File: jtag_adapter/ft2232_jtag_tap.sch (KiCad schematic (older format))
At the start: 50 parts, among them J1 USB_C_Receptacle_USB2.0, J2 Conn_ARM_JTAG_SWD_20, U1 93AA56BT-I/OT, U2 FT232HL, Y1 Crystal_GND24

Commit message: v0.2に改修
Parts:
- removed D1, D2: PGB1010603, Diode_SMD:D_0603_1608Metric, symbol Diode:ESD9B5.0ST5G
- removed R11, R12, R13, R14, R15, R16, R17, R7, R8: 0, Resistor_SMD:R_0603_1608Metric, symbol Device:R
- added D1: PWR_LED, LED_SMD:LED_0603_1608Metric, symbol Device:LED
- added R9: 1k, Resistor_SMD:R_0603_1608Metric, symbol Device:R
- J2: footprint Connector_PinHeader_2.54mm:PinHeader_2x10_P2.54mm_Horizontal -> Connector_IDC:IDC-Header_2x10_P2.54mm_Horizontal
- R8: renamed from R10; value 10k -> 12k/1%
- renumbered R9 to R7
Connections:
- wire segments 198 -> 185
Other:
- note added: "Bypass capacitors for FT232HL"
- note added: "for VCCIO(3.3v)"
- note removed: "Bypass capacitors for FT2232"
- note removed: "dumping resistors"

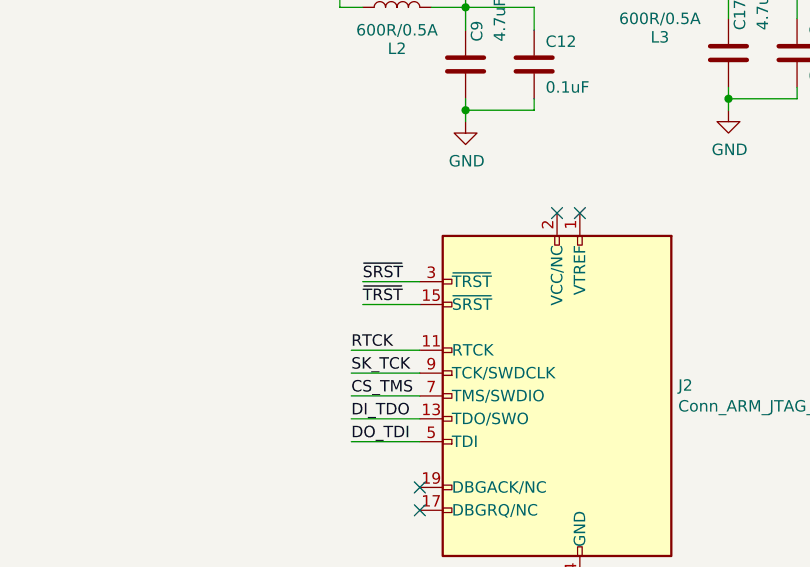
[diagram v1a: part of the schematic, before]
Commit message: fix SRST/TRST and remove unnecessary files
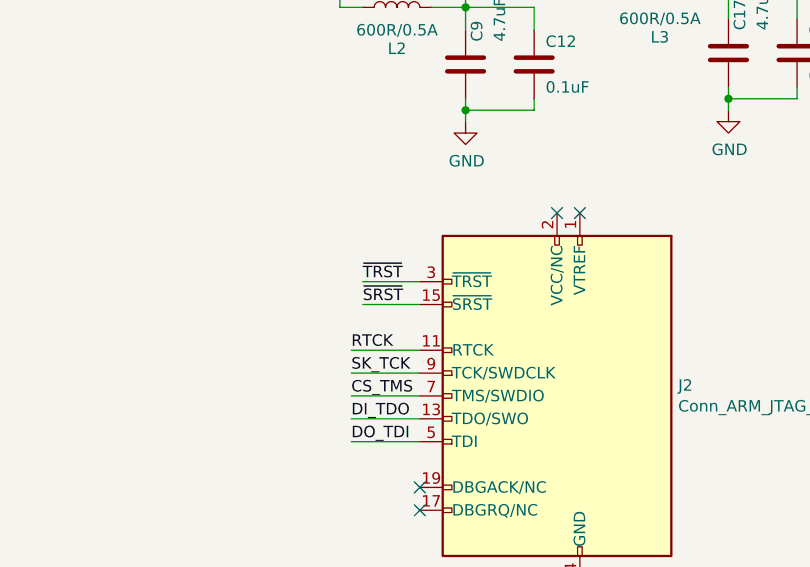
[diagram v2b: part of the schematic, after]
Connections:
- net ~SRST: now also J2.15 (~SRST~); no longer J2.3 (~TRST~)
- net ~TRST: now also J2.3 (~TRST~); no longer J2.15 (~SRST~)
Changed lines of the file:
@@
 Text Label 7650 2650 2    50   ~ 0
 ~TRST
+Text Label 8850 4700 0    50   ~ 0
+~SRST
 Text Label 8850 4600 0    50   ~ 0
-~SRST
-Text Label 8850 4700 0    50   ~ 0
 ~TRST
 Wire Wire Line

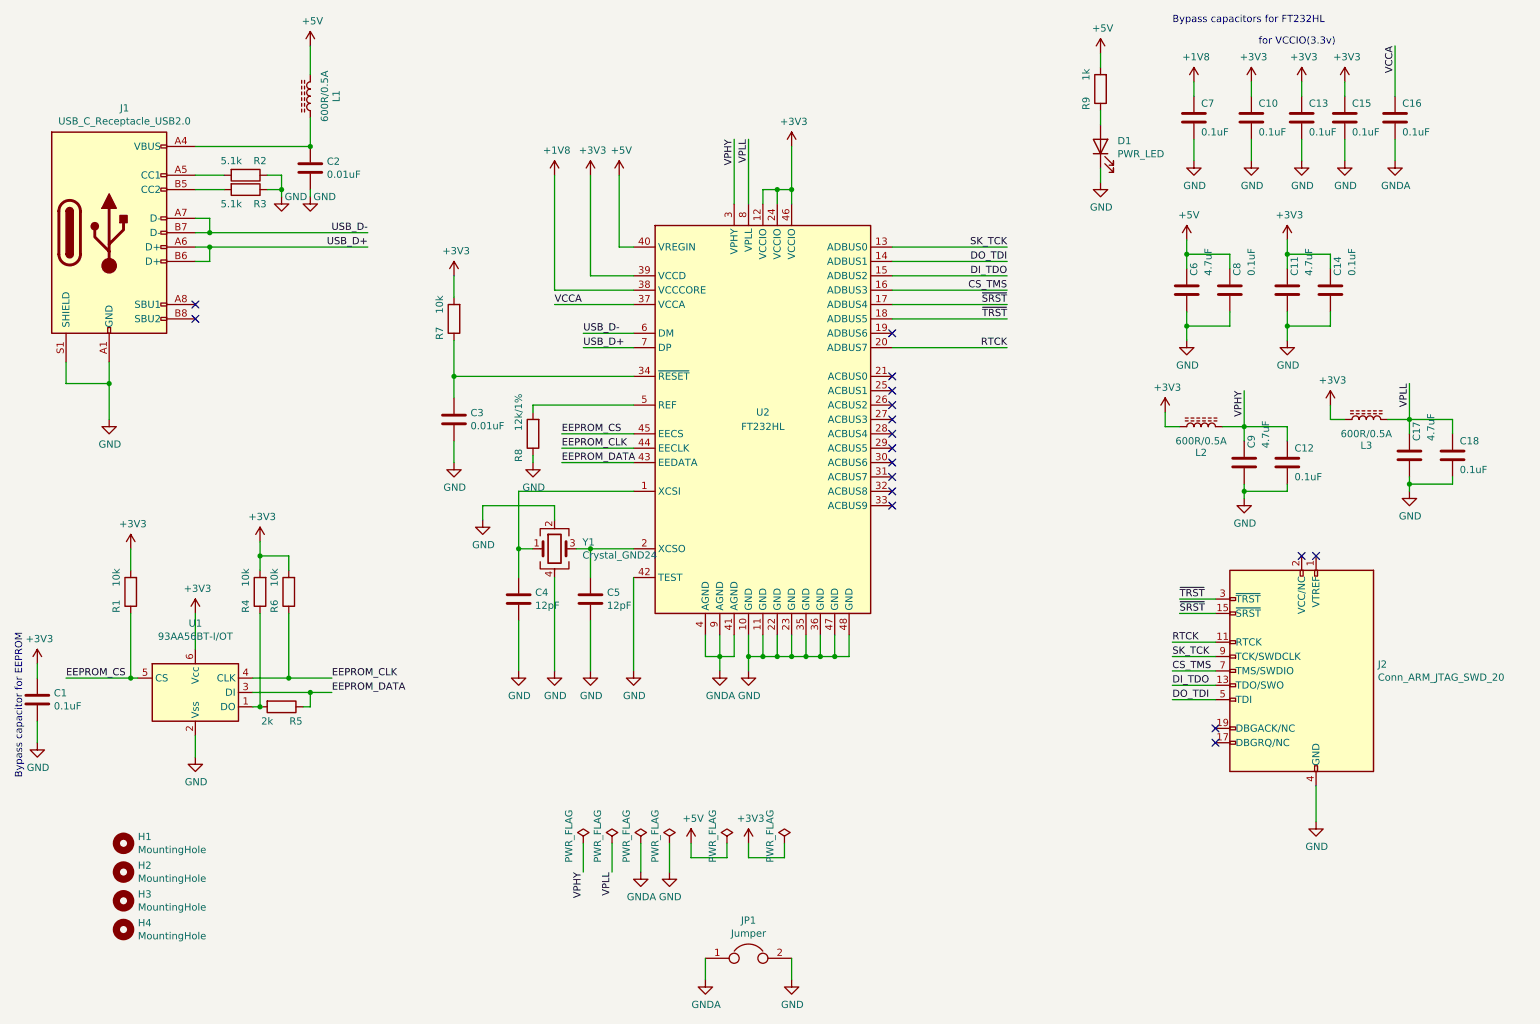
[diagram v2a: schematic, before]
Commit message: wip: 回路図の改善とレベル変換ICの追加
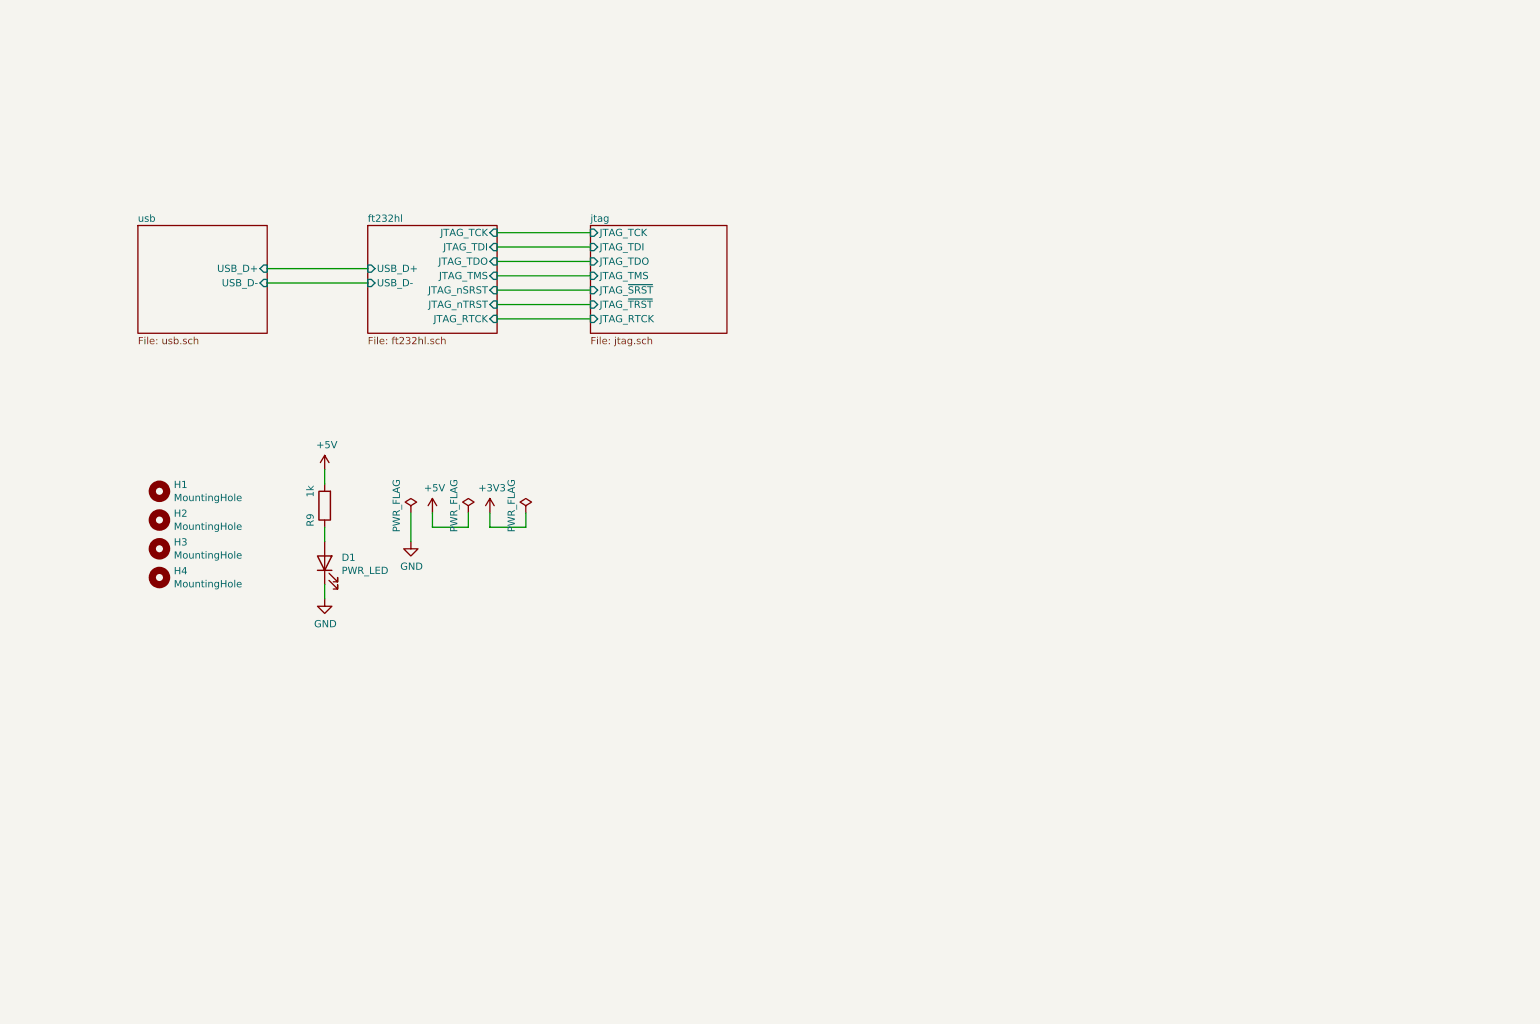
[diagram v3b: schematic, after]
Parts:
- removed C1, C10, C12, C13, C14, C15, C16, C18, C7, C8: 0.1uF, Capacitor_SMD:C_0603_1608Metric, symbol Device:C
- removed C11, C17, C6, C9: 4.7uF, Capacitor_SMD:C_0603_1608Metric, symbol Device:C
- removed C2, C3: 0.01uF, Capacitor_SMD:C_0603_1608Metric, symbol Device:C
- removed C4, C5: 12pF, Capacitor_SMD:C_0603_1608Metric, symbol Device:C
- removed J1: USB_C_Receptacle_USB2.0, Connector_USB:USB_C_Receptacle_GCT_USB4085, symbol Connector:USB_C_Receptacle_USB2.0
- removed J2: Conn_ARM_JTAG_SWD_20, Connector_IDC:IDC-Header_2x10_P2.54mm_Horizontal, symbol Connector:Conn_ARM_JTAG_SWD_20
- removed JP1: Jumper, Jumper:SolderJumper-2_P1.3mm_Bridged_Pad1.0x1.5mm, symbol Device:Jumper
- removed L1, L2, L3: 600R/0.5A, Inductor_SMD:L_0603_1608Metric, symbol Device:L_Core_Ferrite
- removed R1, R4, R6, R7: 10k, Resistor_SMD:R_0603_1608Metric, symbol Device:R
- removed R2, R3: 5.1k, Resistor_SMD:R_0603_1608Metric, symbol Device:R
- removed R5: 2k, Resistor_SMD:R_0603_1608Metric, symbol Device:R
- removed R8: 12k/1%, Resistor_SMD:R_0603_1608Metric, symbol Device:R
- removed U1: 93AA56BT-I/OT, Package_TO_SOT_SMD:SOT-23-6, symbol Memory_EEPROM:93AAxxBT-xOT
- removed U2: FT232HL, Package_QFP:LQFP-48-1EP_7x7mm_P0.5mm_EP3.6x3.6mm, symbol Interface_USB:FT232H
- removed Y1: Crystal_GND24, Crystal:Crystal_SMD_SeikoEpson_FA238-4Pin_3.2x2.5mm, symbol Device:Crystal_GND24
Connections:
- no-connect marks 17 -> 0
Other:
- note removed: "Bypass capacitor for EEPROM"
- note removed: "Bypass capacitors for FT232HL"
- note removed: "for VCCIO(3.3v)"
- moved on the sheet: D1, H1, H2, H3, H4, R9

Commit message: wip
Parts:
- added L1: 600R/0.5A, Inductor_SMD:L_0603_1608Metric, symbol Device:L_Core_Ferrite
- added TP1, TP2, TP3: TestPoint, TestPoint:TestPoint_Pad_D1.0mm, symbol Connector:TestPoint
- renumbered R9 to R1
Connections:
- net +3V3: now also TP3.1
- net +5V: now also TP2.1
- net GND: now also L1.1, TP1.1
- new net GNDA: L1.2
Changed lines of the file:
@@
 encoding utf-8
 Sheet 1 4
-Title ""
-Date ""
-Rev ""
-Comp ""
+Title "FT232 JTAG adapter"
+Date "2021-09-01"
+Rev "v1.0"
+Comp "Toshifumi NISHINAGA(@tnishinaga)"
 Comment1 ""
 Comment2 ""
@@
 $EndDescr
 $Comp
-L power:+5V #PWR023
+L power:+5V #PWR07
 U 1 1 60945E93
-P 3650 4000
-F 0 "#PWR023" H 3650 3850 50  0001 C CNN
-F 1 "+5V" H 3665 4173 50  0000 C CNN
-F 2 "" H 3650 4000 50  0001 C CNN
-F 3 "" H 3650 4000 50  0001 C CNN
-	1    3650 4000
-	1    0    0    -1
+P 4250 4000
+F 0 "#PWR07" H 4250 3850 50  0001 C CNN
+F 1 "+5V" H 4265 4173 50  0000 C CNN
+F 2 "" H 4250 4000 50  0001 C CNN
+F 3 "" H 4250 4000 50  0001 C CNN
+	1    4250 4000
+	1    0    0    -1
+$EndComp
+$Comp
+L power:PWR_FLAG #FLG03
+U 1 1 609471DE
+P 4250 4200
+F 0 "#FLG03" H 4250 4275 50  0001 C CNN
+F 1 "PWR_FLAG" V 4150 4300 50  0000 C CNN
+F 2 "" H 4250 4200 50  0001 C CNN
+F 3 "~" H 4250 4200 50  0001 C CNN
+	1    4250 4200
+	-1   0    0    1
 $EndComp
 $Comp
 L power:PWR_FLAG #FLG04
-U 1 1 609471DE
-P 3900 4000
-F 0 "#FLG04" H 3900 4075 50  0001 C CNN
-F 1 "PWR_FLAG" V 3800 4050 50  0000 C CNN
-F 2 "" H 3900 4000 50  0001 C CNN
-F 3 "~" H 3900 4000 50  0001 C CNN
-	1    3900 4000
-	1    0    0    -1
-$EndComp
-Wire Wire Line
-	3650 4000 3650 4100
-Wire Wire Line
-	3650 4100 3900 4100
-Wire Wire Line
-	3900 4100 3900 4000
-$Comp
-L power:PWR_FLAG #FLG05
 U 1 1 60951BF8
-P 4300 4000
-F 0 "#FLG05" H 4300 4075 50  0001 C CNN
-F 1 "PWR_FLAG" V 4200 4050 50  0000 C CNN
-F 2 "" H 4300 4000 50  0001 C CNN
-F 3 "~" H 4300 4000 50  0001 C CNN
-	1    4300 4000
-	1    0    0    -1
-$EndComp
-$Comp
-L power:+3V3 #PWR027
+P 4700 4200
+F 0 "#FLG04" H 4700 4275 50  0001 C CNN
+F 1 "PWR_FLAG" V 4600 4300 50  0000 C CNN
+F 2 "" H 4700 4200 50  0001 C CNN
+F 3 "~" H 4700 4200 50  0001 C CNN
+	1    4700 4200
+	-1   0    0    1
+$EndComp
+$Comp
+L power:+3V3 #PWR08
 U 1 1 60951E6D
-P 4050 4000
-F 0 "#PWR027" H 4050 3850 50  0001 C CNN
-F 1 "+3V3" H 4065 4173 50  0000 C CNN
-F 2 "" H 4050 4000 50  0001 C CNN
-F 3 "" H 4050 4000 50  0001 C CNN
-	1    4050 4000
-	1    0    0    -1
-$EndComp
-Wire Wire Line
-	4050 4000 4050 4100
-Wire Wire Line
-	4050 4100 4300 4100
-Wire Wire Line
-	4300 4100 4300 4000
+P 4700 4000
+F 0 "#PWR08" H 4700 3850 50  0001 C CNN
+F 1 "+3V3" H 4715 4173 50  0000 C CNN
+F 2 "" H 4700 4000 50  0001 C CNN
+F 3 "" H 4700 4000 50  0001 C CNN
+	1    4700 4000
+	1    0    0    -1
+$EndComp
 $Comp
 L Mechanical:MountingHole H1
@@
 $EndSheet
 $Sheet
-S 3200 2000 900  750
+S 3200 2000 900  1000
 U 61247445
 F0 "ft232hl" 50
@@
 F9 "JTAG_nTRST" I R 4100 2550 50
 F10 "JTAG_RTCK" I R 4100 2650 50
+F11 "SWDIO_OE" I R 4100 2750 50
+F12 "SWD_EN" I R 4100 2850 50
+F13 "JTAG_EN" I R 4100 2950 50
 $EndSheet
 Wire Wire Line
@@
 	3200 2400 2500 2400
 $Sheet
-S 4750 2000 950  750
+S 4750 2000 950  1000
 U 613347ED
 F0 "jtag" 50
@@
 F7 "JTAG_TDO" I L 4750 2250 50
 F8 "JTAG_TDI" I L 4750 2150 50
+F9 "SWDIO_OE" I L 4750 2750 50
+F10 "SWD_EN" I L 4750 2850 50
+F11 "JTAG_EN" I L 4750 2950 50
 $EndSheet
 Wire Wire Line
@@
 	4100 2650 4750 2650
 $Comp
-L power:+5V #PWR030
+L power:+5V #PWR01
 U 1 1 60F3D407
 P 2900 3700
-F 0 "#PWR030" H 2900 3550 50  0001 C CNN
+F 0 "#PWR01" H 2900 3550 50  0001 C CNN
 F 1 "+5V" H 2915 3873 50  0000 C CNN
 F 2 "" H 2900 3700 50  0001 C CNN
@@
 	2900 3700 2900 3800
 $Comp
-L power:GND #PWR031
+L power:GND #PWR02
 U 1 1 60F214BE
 P 2900 4600
-F 0 "#PWR031" H 2900 4350 50  0001 C CNN
+F 0 "#PWR02" H 2900 4350 50  0001 C CNN
 F 1 "GND" H 2905 4427 50  0000 C CNN
 F 2 "" H 2900 4600 50  0001 C CNN
@@
 $EndComp
 $Comp
-L Device:R R9
+L Device:R R1
 U 1 1 60F1735E
 P 2900 3950
-F 0 "R9" V 3000 4050 50  0000 C CNN
+F 0 "R1" V 3000 4050 50  0000 C CNN
 F 1 "1k" V 3000 3850 50  0000 C CNN
 F 2 "Resistor_SMD:R_0603_1608Metric" V 2830 3950 50  0001 C CNN
@@
 $EndComp
 $Comp
-L power:GND #PWR022
+L power:GND #PWR03
 U 1 1 6093156D
 P 3500 4200
-F 0 "#PWR022" H 3500 3950 50  0001 C CNN
+F 0 "#PWR03" H 3500 3950 50  0001 C CNN
 F 1 "GND" H 3505 4027 50  0000 C CNN
 F 2 "" H 3500 4200 50  0001 C CNN
@@
 $EndComp
 Wire Wire Line
-	3500 4200 3500 4000
-$Comp
-L power:PWR_FLAG #FLG03
+	3500 4200 3500 4100
+$Comp
+L power:PWR_FLAG #FLG01
 U 1 1 60931EDC
 P 3500 4000
-F 0 "#FLG03" H 3500 4075 50  0001 C CNN
+F 0 "#FLG01" H 3500 4075 50  0001 C CNN
 F 1 "PWR_FLAG" V 3400 4050 50  0000 C CNN
 F 2 "" H 3500 4000 50  0001 C CNN
@@
 	1    0    0    -1
 $EndComp
+$Comp
+L power:PWR_FLAG #FLG02
+U 1 1 612BB528
+P 4050 4000
+AR Path="/612BB528" Ref="#FLG02"  Part="1"
+AR Path="/61247445/612BB528" Ref="#FLG?"  Part="1"
+F 0 "#FLG02" H 4050 4075 50  0001 C CNN
+F 1 "PWR_FLAG" V 3950 4050 50  0000 C CNN
+F 2 "" H 4050 4000 50  0001 C CNN
+F 3 "~" H 4050 4000 50  0001 C CNN
+	1    4050 4000
+	1    0    0    -1
+$EndComp
+$Comp
+L power:GNDA #PWR05
+U 1 1 612BB52E
+P 4050 4200
+AR Path="/612BB52E" Ref="#PWR05"  Part="1"
+AR Path="/61247445/612BB52E" Ref="#PWR?"  Part="1"
+F 0 "#PWR05" H 4050 3950 50  0001 C CNN
+F 1 "GNDA" H 4055 4027 50  0000 C CNN
+F 2 "" H 4050 4200 50  0001 C CNN
+F 3 "" H 4050 4200 50  0001 C CNN
+	1    4050 4200
+	1    0    0    -1
+$EndComp
+$Comp
+L power:GNDA #PWR04
+U 1 1 612BB535
+P 3500 4900
+AR Path="/612BB535" Ref="#PWR04"  Part="1"
+AR Path="/61247445/612BB535" Ref="#PWR?"  Part="1"
+F 0 "#PWR04" H 3500 4650 50  0001 C CNN
+F 1 "GNDA" H 3505 4727 50  0000 C CNN
+F 2 "" H 3500 4900 50  0001 C CNN
+F 3 "" H 3500 4900 50  0001 C CNN
+	1    3500 4900
+	1    0    0    -1
+$EndComp
+$Comp
+L power:GND #PWR06
+U 1 1 612BB53B
+P 4100 4900
+AR Path="/612BB53B" Ref="#PWR06"  Part="1"
+AR Path="/61247445/612BB53B" Ref="#PWR?"  Part="1"
+F 0 "#PWR06" H 4100 4650 50  0001 C CNN
+F 1 "GND" H 4105 4727 50  0000 C CNN
+F 2 "" H 4100 4900 50  0001 C CNN
+F 3 "" H 4100 4900 50  0001 C CNN
+	1    4100 4900
+	1    0    0    -1
+$EndComp
+Wire Wire Line
+	3500 4900 3500 4750
+Wire Wire Line
+	4100 4750 4100 4900
+$Comp
+L Device:L_Core_Ferrite L1
+U 1 1 612BB544
+P 3800 4750
+AR Path="/612BB544" Ref="L1"  Part="1"
+AR Path="/61247445/612BB544" Ref="L?"  Part="1"
+F 0 "L1" V 3619 4750 50  0000 C CNN
+F 1 "600R/0.5A" V 3700 4750 50  0000 C CNN
+F 2 "Inductor_SMD:L_0603_1608Metric" H 3800 4750 50  0001 C CNN
+F 3 "~" H 3800 4750 50  0001 C CNN
+F 4 "BLM18PG600SN1D" V 3800 4750 50  0001 C CNN "MPN"
+	1    3800 4750
+	0    1    -1   0
+$EndComp
+Wire Wire Line
+	3500 4750 3650 4750
+Wire Wire Line
+	3950 4750 4100 4750
+Wire Wire Line
+	4250 4000 4250 4100
+Wire Wire Line
+	4750 2750 4100 2750
+Wire Wire Line
+	4100 2850 4750 2850
+$Comp
+L Connector:TestPoint TP1
+U 1 1 615BA0CA
+P 3600 4050
+F 0 "TP1" V 3700 4050 50  0000 L CNN
+F 1 "TestPoint" V 3800 4050 50  0000 L CNN
+F 2 "TestPoint:TestPoint_Pad_D1.0mm" H 3800 4050 50  0001 C CNN
+F 3 "~" H 3800 4050 50  0001 C CNN
+	1    3600 4050
+	1    0    0    -1
+$EndComp
+$Comp
+L Connector:TestPoint TP2
+U 1 1 615C08E1
+P 4350 4050
+F 0 "TP2" V 4450 4050 50  0000 L CNN
+F 1 "TestPoint" V 4550 4050 50  0000 L CNN
+F 2 "TestPoint:TestPoint_Pad_D1.0mm" H 4550 4050 50  0001 C CNN
+F 3 "~" H 4550 4050 50  0001 C CNN
+	1    4350 4050
+	1    0    0    -1
+$EndComp
+Wire Wire Line
+	3500 4100 3600 4100
+Wire Wire Line
+	3600 4100 3600 4050
+Connection ~ 3500 4100
+Wire Wire Line
+	3500 4100 3500 4000
+Wire Wire Line
+	4250 4100 4350 4100
+Wire Wire Line
+	4350 4100 4350 4050
+Wire Wire Line
+	4050 4000 4050 4200
+Connection ~ 4250 4100
+Wire Wire Line
+	4250 4100 4250 4200
+$Comp
+L Connector:TestPoint TP3
+U 1 1 615C49CD
+P 4850 4050
+F 0 "TP3" V 4950 4050 50  0000 L CNN
+F 1 "TestPoint" V 5050 4050 50  0000 L CNN
+F 2 "TestPoint:TestPoint_Pad_D1.0mm" H 5050 4050 50  0001 C CNN
+F 3 "~" H 5050 4050 50  0001 C CNN
+	1    4850 4050
+	1    0    0    -1
+$EndComp
+Wire Wire Line
+	4700 4000 4700 4100
+Wire Wire Line
+	4850 4050 4850 4100
+Wire Wire Line
+	4850 4100 4700 4100
+Connection ~ 4700 4100
+Wire Wire Line
+	4700 4100 4700 4200
+Wire Wire Line
+	4100 2950 4750 2950
 $EndSCHEMATC

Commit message: v1.0 基板発注
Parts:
- TP1: value TestPoint -> GND
- TP2: value TestPoint -> +5V
- TP3: value TestPoint -> +3.3V
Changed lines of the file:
@@
 P 3600 4050
 F 0 "TP1" V 3700 4050 50  0000 L CNN
-F 1 "TestPoint" V 3800 4050 50  0000 L CNN
+F 1 "GND" V 3800 4050 50  0000 L CNN
 F 2 "TestPoint:TestPoint_Pad_D1.0mm" H 3800 4050 50  0001 C CNN
 F 3 "~" H 3800 4050 50  0001 C CNN
@@
 P 4350 4050
 F 0 "TP2" V 4450 4050 50  0000 L CNN
-F 1 "TestPoint" V 4550 4050 50  0000 L CNN
+F 1 "+5V" V 4550 4050 50  0000 L CNN
 F 2 "TestPoint:TestPoint_Pad_D1.0mm" H 4550 4050 50  0001 C CNN
 F 3 "~" H 4550 4050 50  0001 C CNN
@@
 P 4850 4050
 F 0 "TP3" V 4950 4050 50  0000 L CNN
-F 1 "TestPoint" V 5050 4050 50  0000 L CNN
+F 1 "+3.3V" V 5050 4050 50  0000 L CNN
 F 2 "TestPoint:TestPoint_Pad_D1.0mm" H 5050 4050 50  0001 C CNN
 F 3 "~" H 5050 4050 50  0001 C CNN

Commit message: wip: stash
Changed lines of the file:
@@
 F11 "SWDIO_OE" I R 4100 2750 50
 F12 "SWD_EN" I R 4100 2850 50
-F13 "JTAG_EN" I R 4100 2950 50
 $EndSheet
 Wire Wire Line
@@
 F9 "SWDIO_OE" I L 4750 2750 50
 F10 "SWD_EN" I L 4750 2850 50
-F11 "JTAG_EN" I L 4750 2950 50
 $EndSheet
 Wire Wire Line
@@
 Wire Wire Line
 	4700 4100 4700 4200
-Wire Wire Line
-	4100 2950 4750 2950
 $EndSCHEMATC
